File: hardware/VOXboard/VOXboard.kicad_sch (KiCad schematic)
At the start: 56 parts, among them J1 USB-C 2.0 16P, J3 AudioJack3, J8 8P8C_LED_Shielded_x4, Q1 2N7002, U1 OPA333, U3 OPA333, U4 STM32F411CEUx, U7 HT7533, Y1 12M

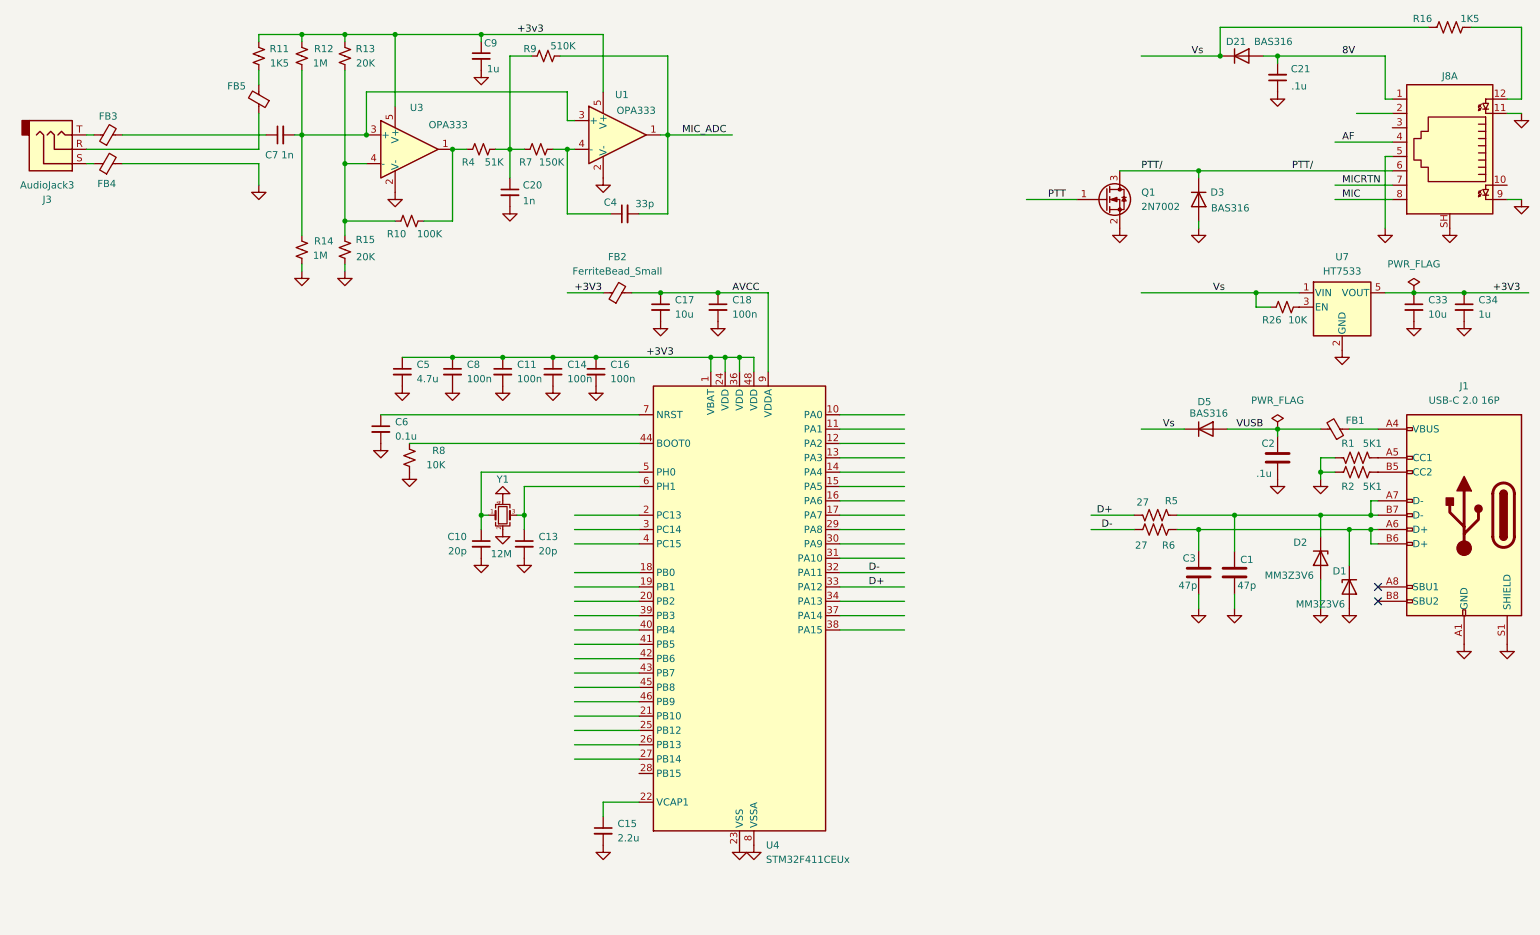
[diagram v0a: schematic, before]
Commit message: Worked on OpAmp design in uSimmics.  Updated schematic.
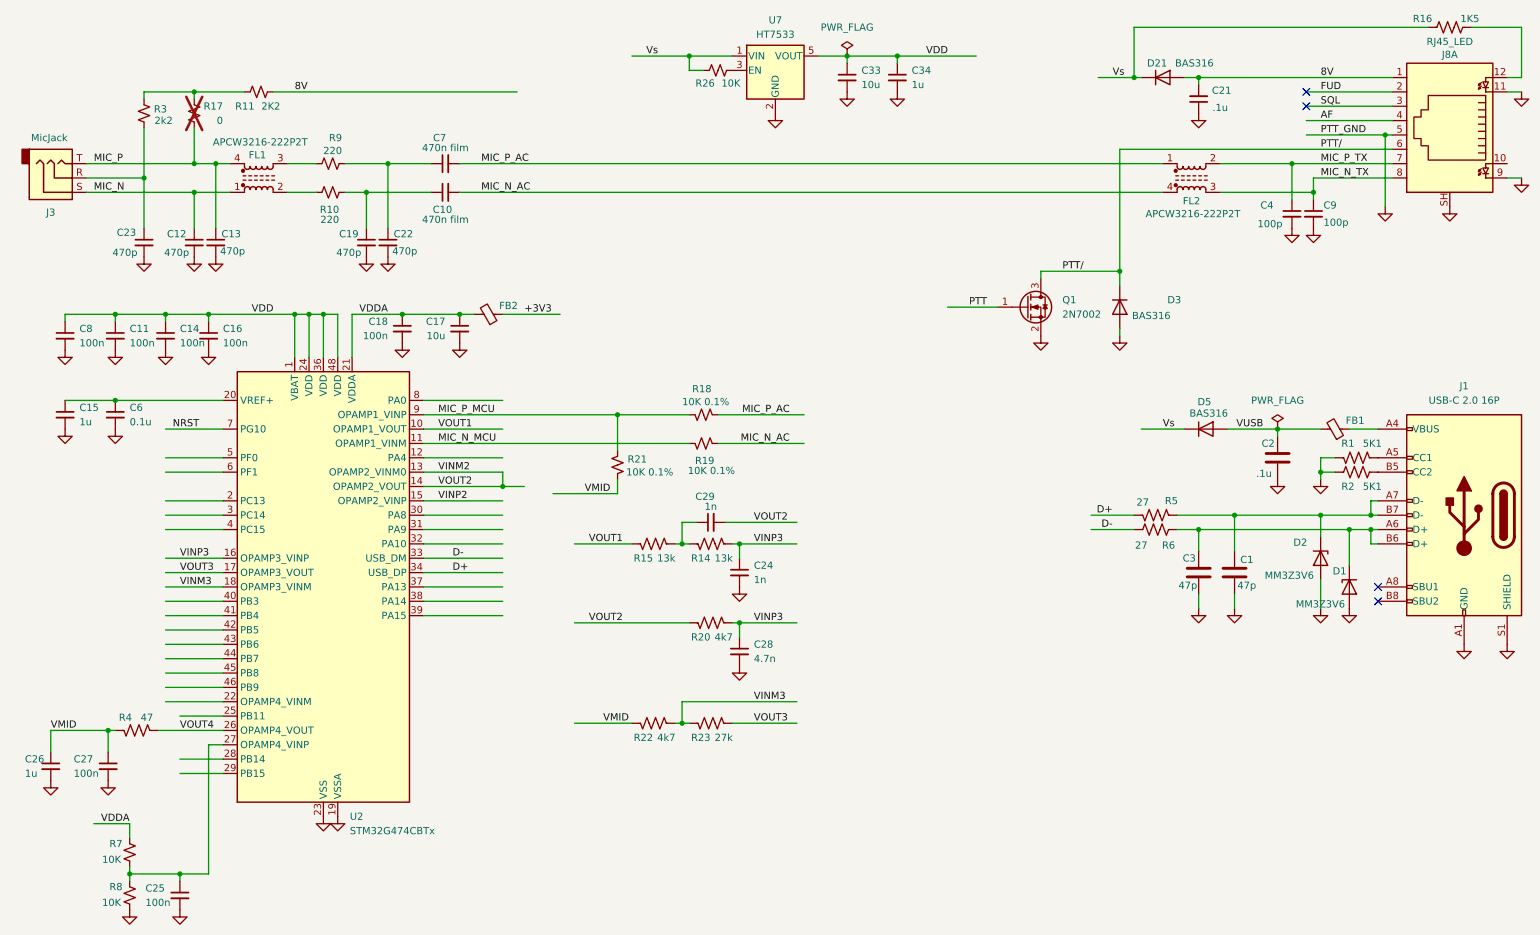
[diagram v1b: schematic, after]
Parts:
- removed C20: 1n, Capacitor_SMD:C_1206_3216Metric_Pad1.33x1.80mm_HandSolder, symbol Device:C_Small
- removed C5: 4.7u, Capacitor_SMD:C_0603_1608Metric, symbol Device:C_Small
- removed FB3: FerriteBead_Small, Connector_RJ:RJ45_Bel_SI-60062-F, symbol Device:FerriteBead_Small
- removed FB4: FerriteBead, symbol Device:FerriteBead_Small
- removed FB5: FerriteBead_Small, symbol Device:FerriteBead_Small
- removed R12, R14: 1M, Resistor_SMD:R_0603_1608Metric, symbol Device:R_Small_US
- removed R13, R15: 20K, Resistor_SMD:R_0603_1608Metric, symbol Device:R_Small_US
- removed R4: 51K, Resistor_SMD:R_0603_1608Metric, symbol Device:R_Small_US
- removed U1, U3: OPA333, Package_TO_SOT_SMD:SOT-23-5, symbol Amplifier_Operational:OPA376xxDBV
- removed U4: STM32F411CEUx, Package_DFN_QFN:QFN-48-1EP_7x7mm_P0.5mm_EP5.6x5.6mm, symbol MCU_ST_STM32F4:STM32F411CEUx
- removed Y1: 12M, Crystal:Crystal_SMD_2016-4Pin_2.0x1.6mm, symbol Device:Crystal_GND24_Small
- added C12, C19, C22, C23: 470p, Capacitor_SMD:C_01005_0402Metric, symbol Device:C_Small
- added C24, C29: 1n, Capacitor_SMD:C_01005_0402Metric, symbol Device:C_Small
- added C25, C27: 100n, Capacitor_SMD:C_01005_0402Metric, symbol Device:C_Small
- added C26: 1u, Capacitor_SMD:C_01005_0402Metric, symbol Device:C_Small
- added C28: 4.7n, Capacitor_SMD:C_01005_0402Metric, symbol Device:C_Small
- added FL1, FL2: APCW3216-222P2T, Inductor_SMD:L_CommonMode_Wurth_WE-CNSW-1206, symbol Filter:0603USB-951
- added R14, R15: 13k, Resistor_SMD:R_01005_0402Metric, symbol Device:R_US
- added R17: 0, Resistor_SMD:R_01005_0402Metric, symbol Device:R_Small_US
- added R18, R19, R21: 10K 0.1%, Resistor_SMD:R_01005_0402Metric, symbol Device:R_Small_US
- added R20, R22: 4k7, Resistor_SMD:R_01005_0402Metric, symbol Device:R_US
- added R23: 27k, Resistor_SMD:R_01005_0402Metric, symbol Device:R_US
- added R3: 2k2, Resistor_SMD:R_01005_0402Metric, symbol Device:R_Small_US
- added R4: 47, Resistor_SMD:R_01005_0402Metric, symbol Device:R_US
- added U2: STM32G474CBTx, Package_QFP:LQFP-48_7x7mm_P0.5mm, symbol MCU_ST_STM32G4:STM32G474CBTx
- C1, C11, C14, C16, C17, C18, C2, C3, C33, C34, C6, C8: footprint Capacitor_SMD:C_0603_1608Metric -> Capacitor_SMD:C_01005_0402Metric
- C10: value 20p -> 470n film; footprint Capacitor_SMD:C_0603_1608Metric -> Capacitor_SMD:C_01005_0402Metric
- C13: value 20p -> 470p; footprint Capacitor_SMD:C_0603_1608Metric -> Capacitor_SMD:C_01005_0402Metric
- C15: value 2.2u -> 1u; footprint Capacitor_SMD:C_0603_1608Metric -> Capacitor_SMD:C_01005_0402Metric
- C21: footprint Capacitor_SMD:C_0402_1005Metric -> Capacitor_SMD:C_01005_0402Metric
- C4: value 33p -> 100p; footprint Capacitor_SMD:C_0603_1608Metric -> Capacitor_SMD:C_01005_0402Metric
- C7: value 1n -> 470n film; footprint Capacitor_SMD:C_0603_1608Metric -> Capacitor_SMD:C_01005_0402Metric
- C9: value 1u -> 100p; footprint Capacitor_SMD:C_1206_3216Metric_Pad1.33x1.80mm_HandSolder -> Capacitor_SMD:C_01005_0402Metric
- FB2: LCSC (none) -> C1017
- J3: value AudioJack3 -> MicJack; footprint (none) -> Connector_Audio:Jack_3.5mm_CUI_SJ1-3513N_Horizontal
- J8: value 8P8C_LED_Shielded_x4 -> RJ45_LED; footprint Connector_RJ:RJ45_Abracon_ARJP11A-MA_Horizontal -> Connector_RJ:RJ45_Amphenol_RJHSE538X
- R1, R16, R2, R26, R8: footprint Resistor_SMD:R_0603_1608Metric -> Resistor_SMD:R_01005_0402Metric
- R10: value 100K -> 220; footprint Resistor_SMD:R_0603_1608Metric -> Resistor_SMD:R_01005_0402Metric
- R11: value 1K5 -> 2K2; footprint Resistor_SMD:R_0603_1608Metric -> Resistor_SMD:R_01005_0402Metric
- R5, R6: footprint Resistor_SMD:R_0402_1005Metric -> Resistor_SMD:R_01005_0402Metric
- R7: value 150K -> 10K; footprint Resistor_SMD:R_0603_1608Metric -> Resistor_SMD:R_01005_0402Metric
- R9: value 510K -> 220; footprint Resistor_SMD:R_0603_1608Metric -> Resistor_SMD:R_01005_0402Metric
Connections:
- net MIC is gone; now on net MIC_N_TX: J8.8
- net MICRTN is gone; now on net MIC_P_TX: J8.7
- net +3V3: no longer C11.1, C14.1, C16.1, C33.1, C34.1, C8.1, U7.5 (VOUT)
- net 8V: now also R11.2
- net D+: now also U2.34 (PA12)
- net D-: now also U2.33 (PA11)
- net GND: now also C4.2, C12.2, C19.2, C22.2, C23.2, C24.2, C25.2, C26.2, C27.2, C28.2, U2.19 (VSSA), U2.23 (VSS), U2.35 (VSS), U2.47 (VSS); no longer C10.2
- net at J3.R: now also C23.1, R3.1
- net MIC_N: now reaches J3.S
- net MIC_N: now also C12.1, FL1.1
- net MIC_P: now reaches J3.T
- net MIC_P: now also C13.1, FL1.4, R17.1
- net at C15.1: now also C6.1, U2.20 (VREF+)
- net at C7.1: now also R9.2, C22.1
- net MIC_P_AC: now reaches C7.2
- net MIC_P_AC: now also FL2.1, R18.1
- net at R7.1: now also R8.2, C25.1, U2.27 (PB13); no longer R9.1
- net MIC_P_TX: now reaches C4.1
- net MIC_P_TX: now also FL2.2; no longer R7.2
- net at R10.1: now also FL1.2
- net at R10.2: now also C10.1, C19.1
- net at R11.1: now also R17.2, R3.2
- net FUD: now reaches J8.2
- net SQL: now reaches J8.3
- net +3v3 renamed MIC_N_TX
- net MIC_N_TX: now also FL2.3; no longer R11.2
- net AVCC renamed VDDA
- net VDDA: now also R7.2, U2.21 (VDDA)
- removed net MIC_ADC: C4.2, R9.2
- new net: FL1.3, R9.1
- new net: C29.1, R14.1, R15.2
- new net MIC_N_AC: C10.2, FL2.4, R19.1
- new net MIC_N_MCU: R19.2, U2.11 (PA3)
- new net MIC_P_MCU: R18.2, R21.2, U2.9 (PA1)
- new net NRST: U2.7 (PG10)
- new net VDD: C11.1, C14.1, C16.1, C33.1, C34.1, C8.1, U2.1 (VBAT), U2.24 (VDD), U2.36 (VDD), U2.48 (VDD), U7.5 (VOUT)
- new net VINM2: C29.2, R20.1, U2.13 (PA5), U2.14 (PA6)
- new net VINM3: R22.2, R23.1, U2.18 (PB2)
- new net VINP2: U2.15 (PA7)
- new net VINP3: C24.1, C28.1, R14.2, R20.2, U2.16 (PB0)
- new net VMID: C26.1, C27.1, R21.1, R22.1, R4.1
- new net VOUT1: R15.1, U2.10 (PA2)
- new net VOUT3: R23.2, U2.17 (PB1)
- new net VOUT4: R4.2, U2.26 (PB12)
- no-connect marks 2 -> 4
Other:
- moved on the sheet: C11, C14, C16, C17, C18, C21, C33, C34, C6, C7, C8, D21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
